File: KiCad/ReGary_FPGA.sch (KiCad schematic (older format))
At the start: 28 parts, among them U1 GW1N-UV1P5LQ100, U2 LM1117-3.3, U3 TPS73643DBV

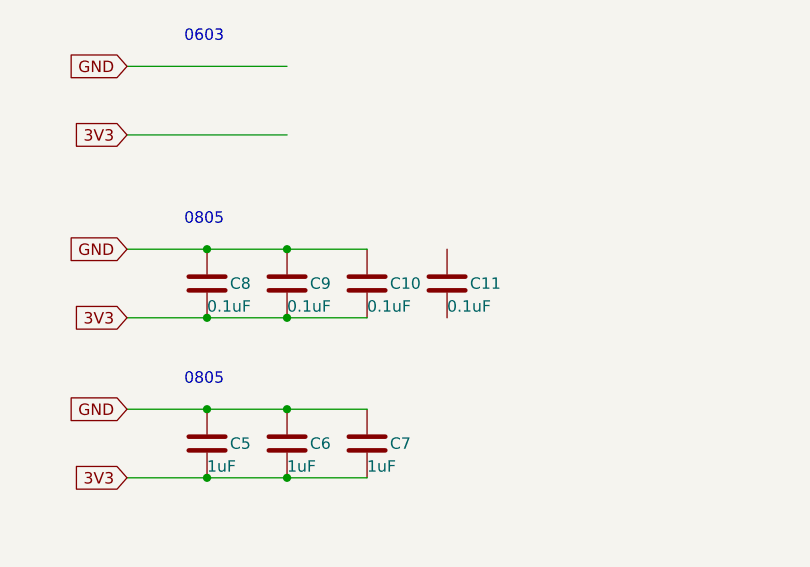
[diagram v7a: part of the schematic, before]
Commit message: fixed placement of capacitors C9,C10 and resistor array RN1
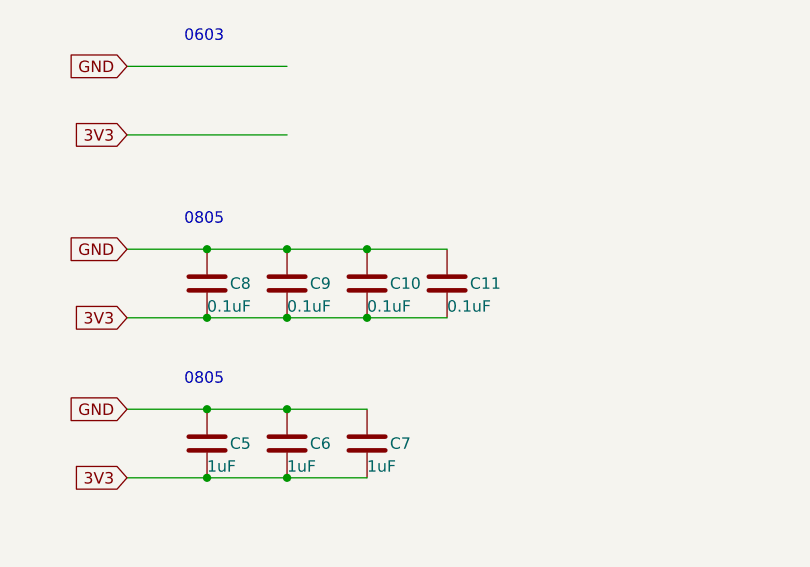
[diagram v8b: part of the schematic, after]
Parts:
- C11: footprint Capacitor_SMD:C_0805_2012Metric_Pad1.15x1.40mm_HandSolder -> Capacitor_SMD:C_0805_2012Metric_Pad1.18x1.45mm_HandSolder
- C12, C13, C14, C15, C16, C17, C18, C19: footprint Capacitor_SMD:C_0603_1608Metric_Pad1.05x0.95mm_HandSolder -> Capacitor_SMD:C_0603_1608Metric_Pad1.08x0.95mm_HandSolder
- C9: renamed from C10; footprint Capacitor_SMD:C_0805_2012Metric_Pad1.15x1.40mm_HandSolder -> Capacitor_SMD:C_0805_2012Metric_Pad1.18x1.45mm_HandSolder
- renumbered C9 to C10
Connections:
- wire segments 57 -> 59
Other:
- moved on the sheet: C10, C9
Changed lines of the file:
@@
 F 0 "C19" H 9800 3750 50  0000 L CNN
 F 1 "0.01uF" H 9700 3650 50  0000 L CNN
-F 2 "Capacitor_SMD:C_0603_1608Metric_Pad1.05x0.95mm_HandSolder" H 9738 3600 50  0001 C CNN
+F 2 "Capacitor_SMD:C_0603_1608Metric_Pad1.08x0.95mm_HandSolder" H 9738 3600 50  0001 C CNN
 F 3 "~" H 9700 3750 50  0001 C CNN
 	1    9700 3750
@@
 F 0 "C18" H 9450 3750 50  0000 L CNN
 F 1 "0.01uF" H 9350 3650 50  0000 L CNN
-F 2 "Capacitor_SMD:C_0603_1608Metric_Pad1.05x0.95mm_HandSolder" H 9388 3600 50  0001 C CNN
+F 2 "Capacitor_SMD:C_0603_1608Metric_Pad1.08x0.95mm_HandSolder" H 9388 3600 50  0001 C CNN
 F 3 "~" H 9350 3750 50  0001 C CNN
 	1    9350 3750
@@
 L Device:C C?
 U 1 1 60CC8F0E
-P 8300 5300
+P 7950 5300
 AR Path="/60CC8F0E" Ref="C?"  Part="1"
-AR Path="/608A10F5/60CC8F0E" Ref="C10"  Part="1"
-F 0 "C10" H 8400 5300 50  0000 L CNN
-F 1 "0.1uF" H 8300 5200 50  0000 L CNN
-F 2 "Capacitor_SMD:C_0805_2012Metric_Pad1.15x1.40mm_HandSolder" H 8338 5150 50  0001 C CNN
-F 3 "~" H 8300 5300 50  0001 C CNN
-	1    8300 5300
+AR Path="/608A10F5/60CC8F0E" Ref="C9"  Part="1"
+F 0 "C9" H 8050 5300 50  0000 L CNN
+F 1 "0.1uF" H 7950 5200 50  0000 L CNN
+F 2 "Capacitor_SMD:C_0805_2012Metric_Pad1.18x1.45mm_HandSolder" H 7988 5150 50  0001 C CNN
+F 3 "~" H 7950 5300 50  0001 C CNN
+	1    7950 5300
 	1    0    0    -1
 $EndComp
@@
 F 0 "C11" H 8750 5300 50  0000 L CNN
 F 1 "0.1uF" H 8650 5200 50  0000 L CNN
-F 2 "Capacitor_SMD:C_0805_2012Metric_Pad1.15x1.40mm_HandSolder" H 8688 5150 50  0001 C CNN
+F 2 "Capacitor_SMD:C_0805_2012Metric_Pad1.18x1.45mm_HandSolder" H 8688 5150 50  0001 C CNN
 F 3 "~" H 8650 5300 50  0001 C CNN
 	1    8650 5300
@@
 F 0 "C12" H 7350 3750 50  0000 L CNN
 F 1 "0.01uF" H 7250 3650 50  0000 L CNN
-F 2 "Capacitor_SMD:C_0603_1608Metric_Pad1.05x0.95mm_HandSolder" H 7288 3600 50  0001 C CNN
+F 2 "Capacitor_SMD:C_0603_1608Metric_Pad1.08x0.95mm_HandSolder" H 7288 3600 50  0001 C CNN
 F 3 "~" H 7250 3750 50  0001 C CNN
 	1    7250 3750
@@
 F 0 "C13" H 7700 3750 50  0000 L CNN
 F 1 "0.01uF" H 7600 3650 50  0000 L CNN
-F 2 "Capacitor_SMD:C_0603_1608Metric_Pad1.05x0.95mm_HandSolder" H 7638 3600 50  0001 C CNN
+F 2 "Capacitor_SMD:C_0603_1608Metric_Pad1.08x0.95mm_HandSolder" H 7638 3600 50  0001 C CNN
 F 3 "~" H 7600 3750 50  0001 C CNN
 	1    7600 3750
@@
 F 0 "C15" H 8400 3750 50  0000 L CNN
 F 1 "0.01uF" H 8300 3650 50  0000 L CNN
-F 2 "Capacitor_SMD:C_0603_1608Metric_Pad1.05x0.95mm_HandSolder" H 8338 3600 50  0001 C CNN
+F 2 "Capacitor_SMD:C_0603_1608Metric_Pad1.08x0.95mm_HandSolder" H 8338 3600 50  0001 C CNN
 F 3 "~" H 8300 3750 50  0001 C CNN
 	1    8300 3750
@@
 F 0 "C16" H 8750 3750 50  0000 L CNN
 F 1 "0.01uF" H 8650 3650 50  0000 L CNN
-F 2 "Capacitor_SMD:C_0603_1608Metric_Pad1.05x0.95mm_HandSolder" H 8688 3600 50  0001 C CNN
+F 2 "Capacitor_SMD:C_0603_1608Metric_Pad1.08x0.95mm_HandSolder" H 8688 3600 50  0001 C CNN
 F 3 "~" H 8650 3750 50  0001 C CNN
 	1    8650 3750
@@
 L Device:C C?
 U 1 1 608291F3
-P 7950 5300
+P 8300 5300
 AR Path="/608291F3" Ref="C?"  Part="1"
-AR Path="/608A10F5/608291F3" Ref="C9"  Part="1"
-F 0 "C9" H 8050 5300 50  0000 L CNN
-F 1 "0.1uF" H 7950 5200 50  0000 L CNN
-F 2 "Capacitor_SMD:C_0805_2012Metric_Pad1.18x1.45mm_HandSolder" H 7988 5150 50  0001 C CNN
-F 3 "~" H 7950 5300 50  0001 C CNN
-	1    7950 5300
+AR Path="/608A10F5/608291F3" Ref="C10"  Part="1"
+F 0 "C10" H 8400 5300 50  0000 L CNN
+F 1 "0.1uF" H 8300 5200 50  0000 L CNN
+F 2 "Capacitor_SMD:C_0805_2012Metric_Pad1.18x1.45mm_HandSolder" H 8338 5150 50  0001 C CNN
+F 3 "~" H 8300 5300 50  0001 C CNN
+	1    8300 5300
 	1    0    0    -1
 $EndComp
@@
 F 0 "C17" H 9100 3750 50  0000 L CNN
 F 1 "0.01uF" H 9000 3650 50  0000 L CNN
-F 2 "Capacitor_SMD:C_0603_1608Metric_Pad1.05x0.95mm_HandSolder" H 9038 3600 50  0001 C CNN
+F 2 "Capacitor_SMD:C_0603_1608Metric_Pad1.08x0.95mm_HandSolder" H 9038 3600 50  0001 C CNN
 F 3 "~" H 9000 3750 50  0001 C CNN
 	1    9000 3750
@@
 F 0 "C14" H 8050 3750 50  0000 L CNN
 F 1 "0.01uF" H 7950 3650 50  0000 L CNN
-F 2 "Capacitor_SMD:C_0603_1608Metric_Pad1.05x0.95mm_HandSolder" H 7988 3600 50  0001 C CNN
+F 2 "Capacitor_SMD:C_0603_1608Metric_Pad1.08x0.95mm_HandSolder" H 7988 3600 50  0001 C CNN
 F 3 "~" H 7950 3750 50  0001 C CNN
 	1    7950 3750
@@
 Wire Wire Line
 	8800 2550 8600 2550
+Wire Wire Line
+	8300 5150 8650 5150
+Connection ~ 8300 5150
+Wire Wire Line
+	8300 5450 8650 5450
+Connection ~ 8300 5450
 $EndSCHEMATC
